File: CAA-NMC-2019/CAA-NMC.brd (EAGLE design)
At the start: 33.3 x 50.2 mm, 147 parts, among them IC1 ATTINY85-20SU, J1 M20-9980346

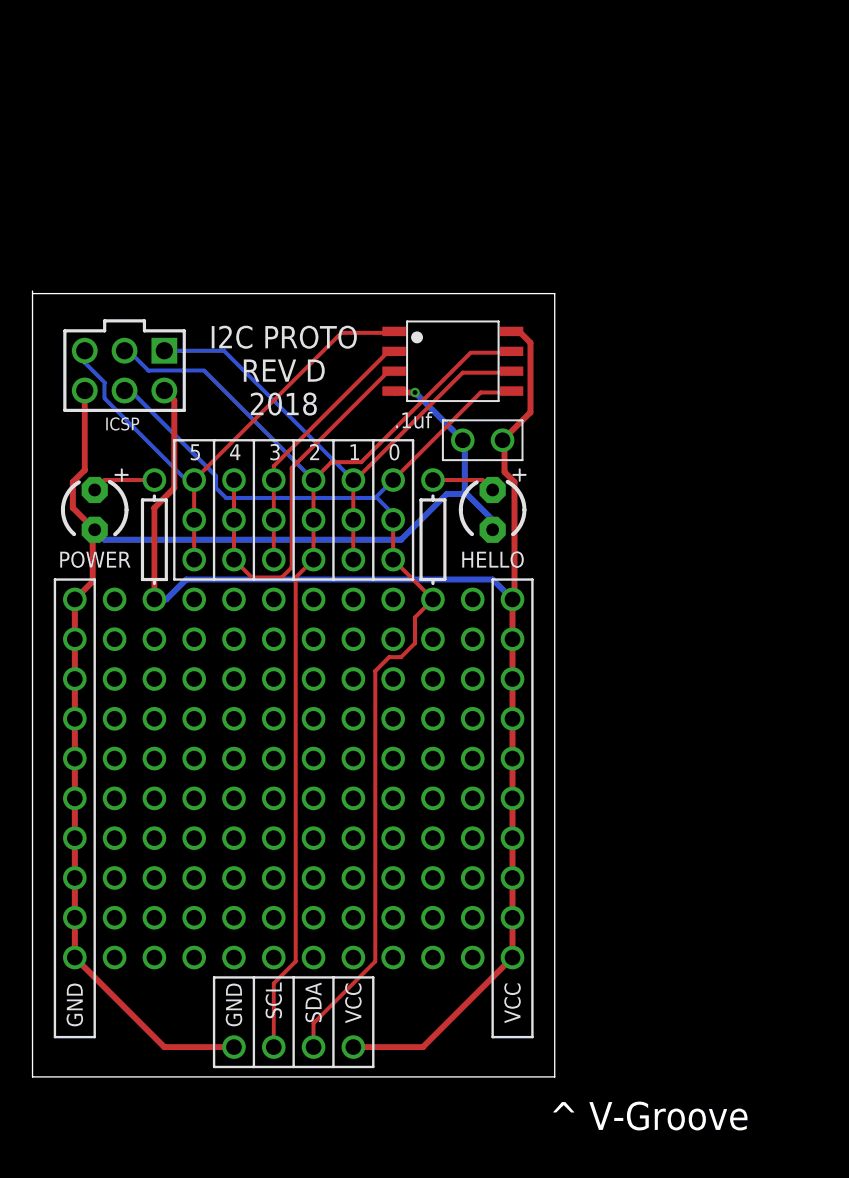
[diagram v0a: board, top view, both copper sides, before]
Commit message: added smt battery mount
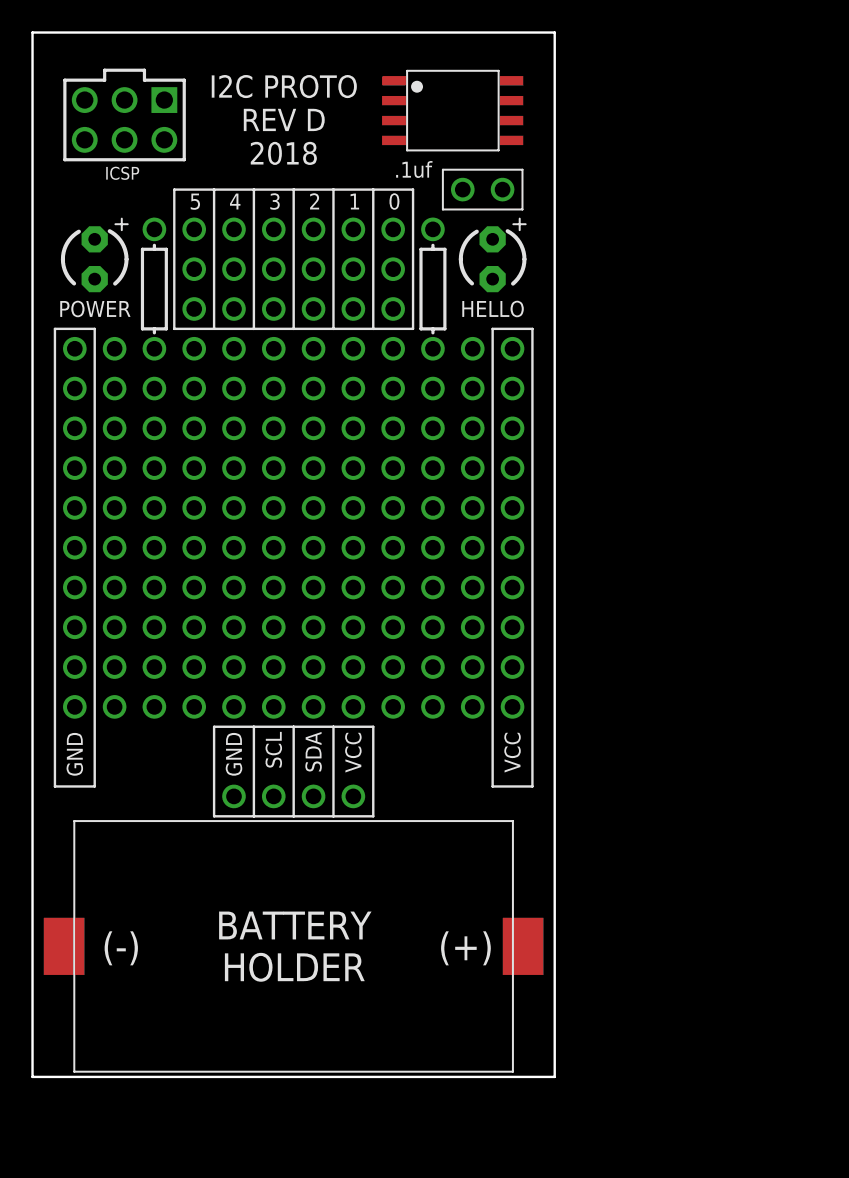
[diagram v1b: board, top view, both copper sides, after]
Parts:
- added U$144: SMT-BATTERY-HOLDER, BadgeParts:SMT-CR-HOLDER
- moved HELLO 16.0 mm to (29.4, 52.2)
- moved IC1 16.0 mm to (26.8, 61.7)
- moved J1 16.0 mm to (5.88, 58.5)
- moved POWER 16.0 mm to (3.97, 52.2)
- moved U$10 16.0 mm to (7.78, 28.7)
- moved U$101 16.0 mm to (10.3, 41.4)
- moved U$105 16.0 mm to (12.9, 41.4)
- moved U$109 16.0 mm to (15.4, 41.4)
- moved U$11 16.0 mm to (7.78, 36.3)
- moved U$113 16.0 mm to (17.9, 41.4)
- moved U$116 16.0 mm to (25.6, 41.4)
- moved U$117 16.0 mm to (20.5, 41.4)
- moved U$12 16.0 mm to (7.78, 26.2)
- moved U$120 16.0 mm to (28.1, 41.4)
- moved U$121 16.0 mm to (23.0, 41.4)
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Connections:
- net GND: now also U$144.GND
- net VCC: now also U$144.VCC
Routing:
- net VCC: track 92.4 -> 0.00 mm
- net GND: track 87.5 -> 0.00 mm, vias 1 -> 0
- net PB0: track 71.0 -> 0.00 mm
- net PB2: track 68.8 -> 0.00 mm
- net PB1: track 33.5 -> 0.00 mm
- net PB5: track 33.2 -> 0.00 mm
- net PB4: track 25.0 -> 0.00 mm
- net PB3: track 16.7 -> 0.00 mm
- net N$2: track 4.07 -> 0.00 mm
- net N$1: track 4.07 -> 0.00 mm
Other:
- board size 33.3 x 50.2 mm -> 33.3 x 66.7 mm
- board text removed: "^ V-Groove"

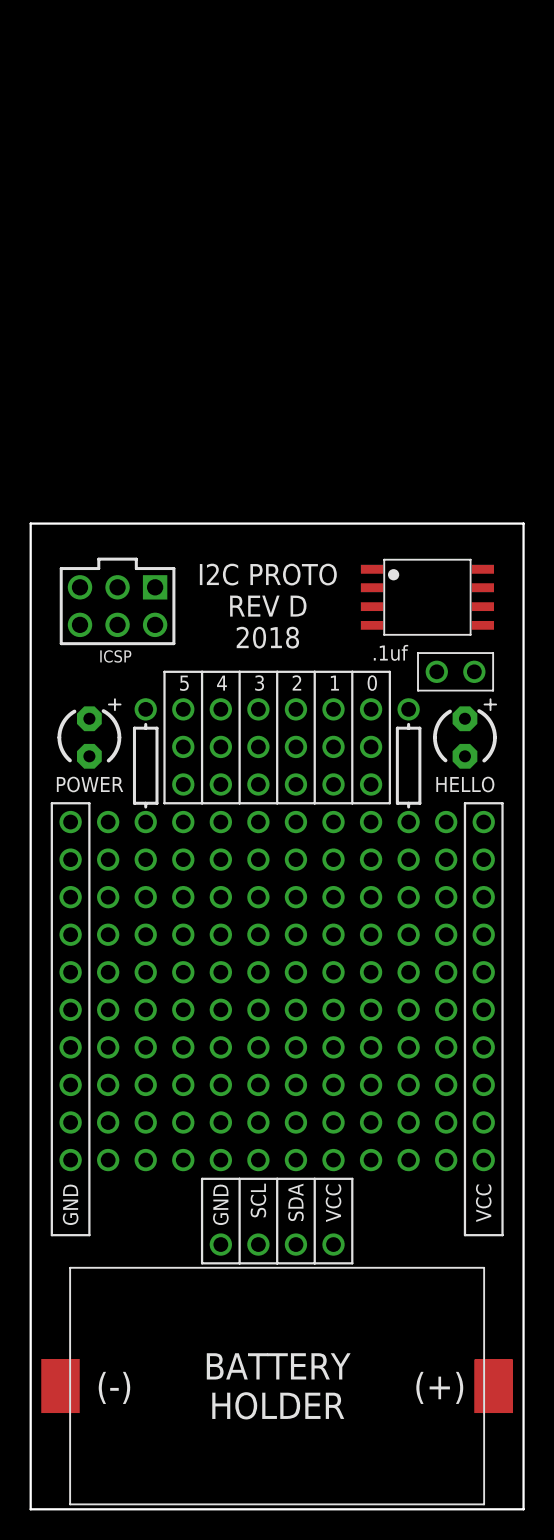
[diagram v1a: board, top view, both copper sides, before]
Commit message: Change dim to meet seeed rqmts
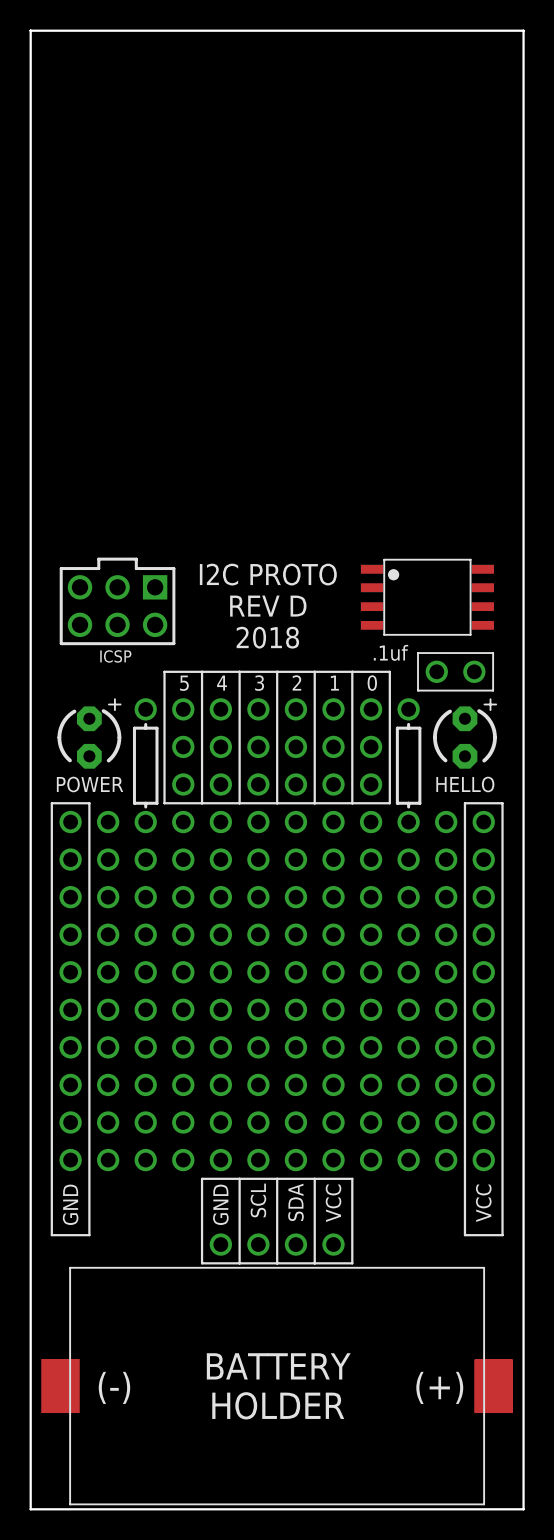
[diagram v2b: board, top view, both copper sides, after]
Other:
- board size 33.3 x 66.7 mm -> 33.3 x 100 mm
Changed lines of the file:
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@@
 <setting verticaltext="up"/>
 </settings>
-<grid distance="1" unitdist="mm" unit="mm" style="lines" multiple="1" display="yes" altdistance="0.003125" altunitdist="mic" altunit="mm"/>
+<grid distance="33.333" unitdist="mm" unit="mm" style="lines" multiple="1" display="yes" altdistance="0.003125" altunitdist="mic" altunit="mm"/>
 <layers>
 <layer number="1" name="Top" color="4" fill="1" visible="yes" active="yes"/>
@@
 <layer number="18" name="Vias" color="2" fill="1" visible="yes" active="yes"/>
 <layer number="19" name="Unrouted" color="6" fill="1" visible="yes" active="yes"/>
-<layer number="20" name="Dimension" color="24" fill="1" visible="no" active="yes"/>
+<layer number="20" name="Dimension" color="24" fill="1" visible="yes" active="yes"/>
 <layer number="21" name="tPlace" color="7" fill="1" visible="yes" active="yes"/>
-<layer number="22" name="bPlace" color="7" fill="1" visible="yes" active="yes"/>
+<layer number="22" name="bPlace" color="7" fill="1" visible="no" active="yes"/>
 <layer number="23" name="tOrigins" color="15" fill="1" visible="yes" active="yes"/>
 <layer number="24" name="bOrigins" color="15" fill="1" visible="yes" active="yes"/>
@@
 <wire x1="31.91" y1="47.75" x2="29.37" y2="47.75" width="0.1524" layer="21"/>
 <wire x1="29.37" y1="47.75" x2="29.37" y2="18.54" width="0.1524" layer="21"/>
-<wire x1="0" y1="66.666" x2="0" y2="0" width="0.1524" layer="20"/>
-<wire x1="0" y1="0" x2="33.333" y2="0" width="0.1524" layer="20"/>
-<wire x1="33.333" y1="0" x2="33.333" y2="66.666" width="0.1524" layer="20"/>
-<wire x1="33.333" y1="66.666" x2="0" y2="66.666" width="0.1524" layer="20"/>
+<wire x1="0" y1="0" x2="0" y2="99.999" width="0.1524" layer="20"/>
+<wire x1="0" y1="99.999" x2="0" y2="100" width="0.1524" layer="20"/>
+<wire x1="0" y1="99.999" x2="33.333" y2="99.999" width="0.1524" layer="20"/>
+<wire x1="33.333" y1="99.999" x2="33.333" y2="0" width="0.1524" layer="20"/>
+<wire x1="33.333" y1="0" x2="0" y2="0" width="0.1524" layer="20"/>
 </plain>
 <attributes>

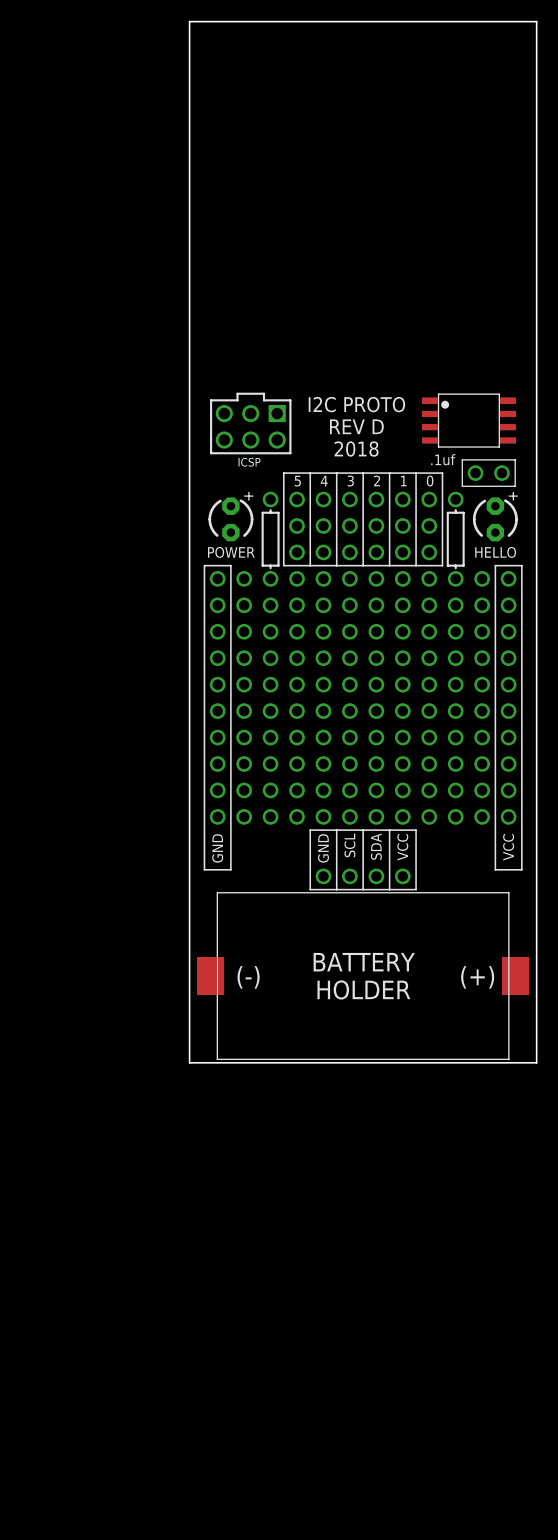
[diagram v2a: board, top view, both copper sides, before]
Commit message: added lanyard hole, 3 RGB LEDs
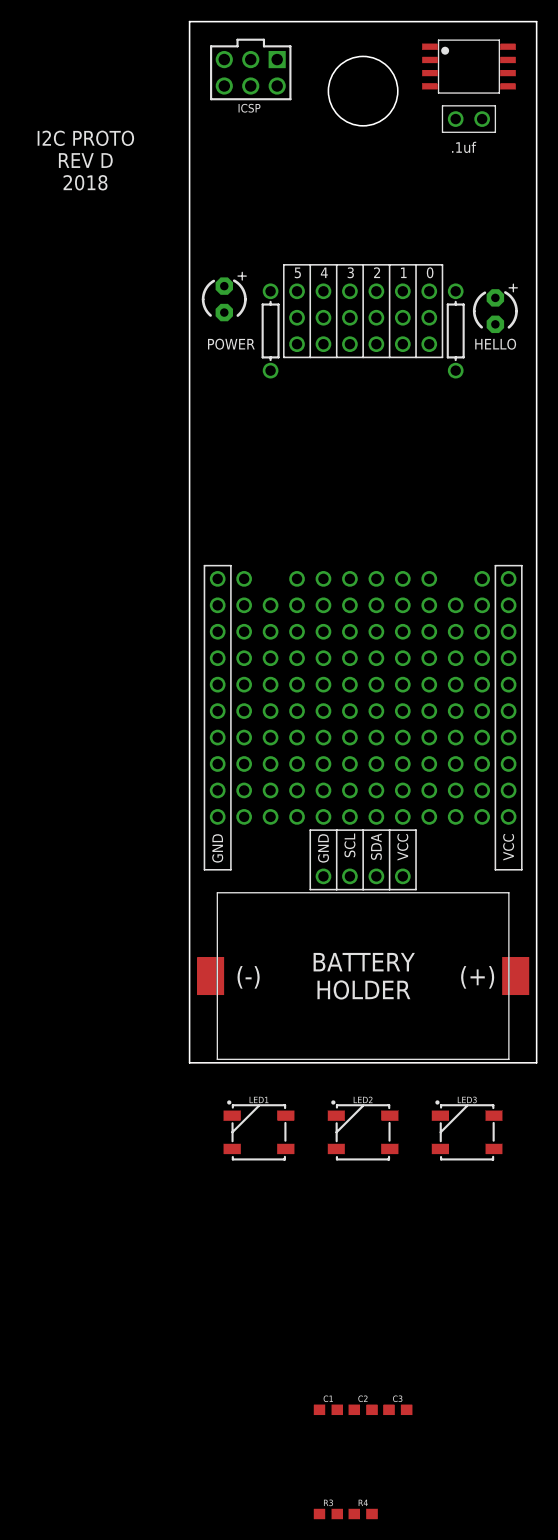
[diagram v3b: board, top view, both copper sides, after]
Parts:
- added C1, C2, C3: 0.1uF, SparkFun-Capacitors:0603
- added LED1, LED2, LED3: WS2812B, SparkFun-LED:WS2812B
- added R3: 470, SparkFun-Resistors:0603
- added R4: 10k, SparkFun-Resistors:0603
- moved U$123 34.1 mm to (25.6, 90.6)
- moved IC1 34.0 mm to (26.8, 95.7)
- moved J1 34.0 mm to (5.88, 92.5)
- moved POWER 21.1 mm to (3.33, 73.3)
- moved U$126 20.0 mm to (7.78, 70.3)
- moved U$127 20.0 mm to (25.6, 70.3)
- moved U$76 20.0 mm to (23.0, 71.6)
- moved U$79 20.0 mm to (20.5, 71.6)
- moved U$83 20.0 mm to (17.9, 71.6)
- moved U$86 20.0 mm to (15.4, 71.6)
- moved U$87 20.0 mm to (12.9, 71.6)
- moved U$90 20.0 mm to (10.3, 71.6)
- moved HELLO 20.0 mm to (29.4, 72.2)
- moved U$75 20.0 mm to (23.0, 74.1)
- moved U$77 20.0 mm to (23.0, 69.0)
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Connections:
- new net N$10: LED2.2, LED3.4
- new net N$12: LED1.4, R3.1
- new net N$9: LED1.2, LED2.4
- new net RGBLEDS: R3.2, R4.1
- new net VDD: C1.1, C2.1, C3.1, LED1.1, LED2.1, LED3.1, R4.2
- net GND: now also C1.2, C2.2, C3.2, LED1.3, LED2.3, LED3.3
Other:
- outline, holes or cut-outs redrawn

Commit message: breathing room for redesign
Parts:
- moved U$75 30.0 mm to (53.0, 74.1)
- moved U$76 30.0 mm to (53.0, 71.6)
- moved U$77 30.0 mm to (53.0, 69.0)
- moved U$84 30.0 mm to (45.4, 74.1)
- moved U$85 30.0 mm to (45.4, 69.0)
- moved U$86 30.0 mm to (45.4, 71.6)
- moved U$87 30.0 mm to (42.9, 71.6)
- moved U$88 30.0 mm to (42.9, 74.1)
- moved U$89 30.0 mm to (42.9, 69.0)
- moved U$90 30.0 mm to (40.3, 71.6)
- moved U$91 30.0 mm to (40.3, 74.1)
- moved U$92 30.0 mm to (40.3, 69.0)
- moved U$78 30.0 mm to (50.5, 74.1)
- moved U$79 30.0 mm to (50.5, 71.6)
- moved U$80 30.0 mm to (50.5, 69.0)
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
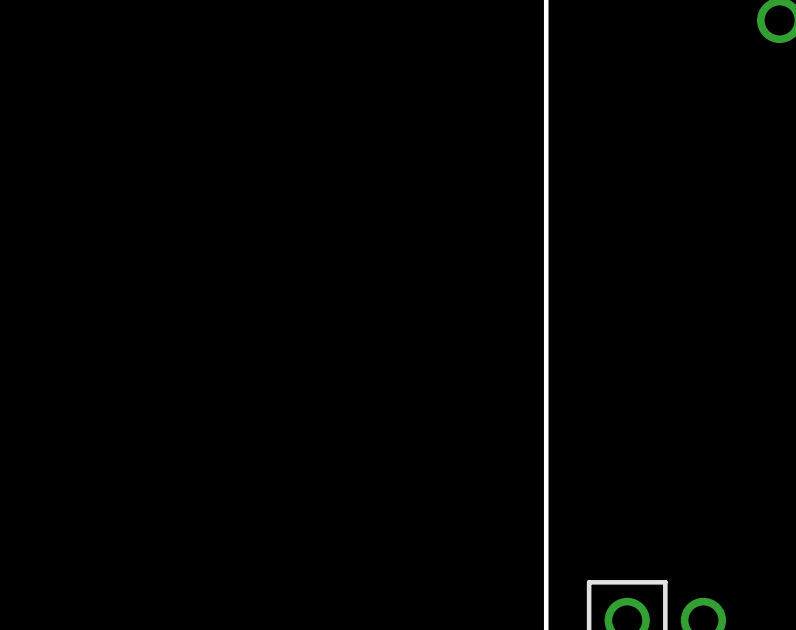
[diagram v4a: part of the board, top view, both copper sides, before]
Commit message: added SMT switch to design/lbr
This can be used as on/off for battery, but should also be wired to isolate battery voltage from USB
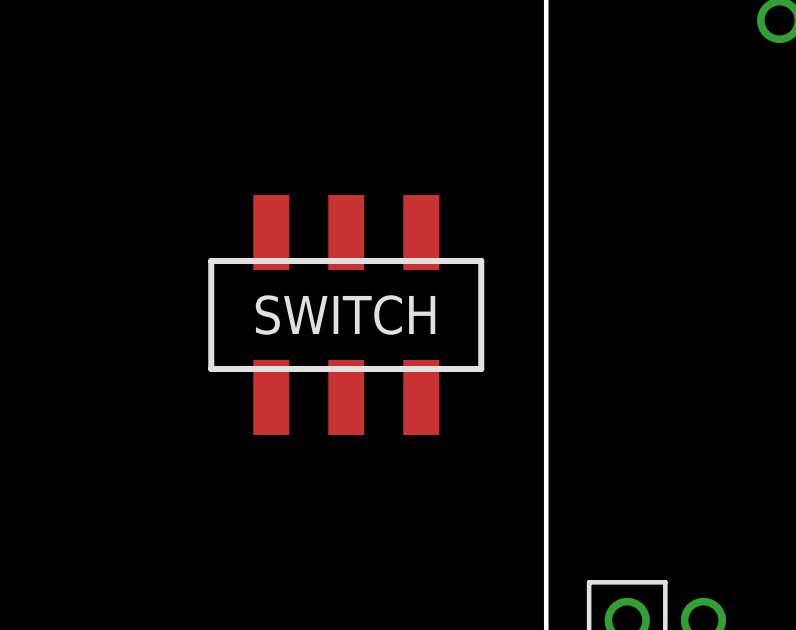
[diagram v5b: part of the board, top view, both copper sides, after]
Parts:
- added U$145: SMT-SWITCH, BadgeParts:SMT-SWITCH
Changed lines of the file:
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@@
 <attribute name="VALUE" x="16.665" y="-44.091" size="0.6096" layer="27" font="vector" ratio="20" align="top-center"/>
 </element>
+<element name="U$145" library="BadgeParts" package="SMT-SWITCH" value="SMT-SWITCH" x="-6.666" y="56.661" smashed="yes"/>
 </elements>
 <signals>
